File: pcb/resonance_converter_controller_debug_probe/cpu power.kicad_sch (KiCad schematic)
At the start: 9 parts, among them U30 OSD32MP157C-512M-BAA

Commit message: Add schematic for debug probe
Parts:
- TP1, TP2, TP3, TP4, TP5, TP6, TP7, TP8: footprint (none) -> TestPoint:TestPoint_Pad_D1.0mm
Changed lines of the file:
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@@
 			)
 		)
-		(property "Footprint" ""
+		(property "Footprint" "TestPoint:TestPoint_Pad_D1.0mm"
 			(at 106.68 123.19 0)
 			(effects
@@
 			)
 		)
-		(property "Footprint" ""
+		(property "Footprint" "TestPoint:TestPoint_Pad_D1.0mm"
 			(at 106.68 85.09 0)
 			(effects
@@
 			)
 		)
-		(property "Footprint" ""
+		(property "Footprint" "TestPoint:TestPoint_Pad_D1.0mm"
 			(at 118.11 26.67 0)
 			(effects
@@
 			)
 		)
-		(property "Footprint" ""
+		(property "Footprint" "TestPoint:TestPoint_Pad_D1.0mm"
 			(at 118.11 57.15 0)
 			(effects
@@
 			)
 		)
-		(property "Footprint" ""
+		(property "Footprint" "TestPoint:TestPoint_Pad_D1.0mm"
 			(at 106.68 110.49 0)
 			(effects
@@
 			)
 		)
-		(property "Footprint" ""
+		(property "Footprint" "TestPoint:TestPoint_Pad_D1.0mm"
 			(at 118.11 41.91 0)
 			(effects
@@
 			)
 		)
-		(property "Footprint" ""
+		(property "Footprint" "TestPoint:TestPoint_Pad_D1.0mm"
 			(at 106.68 97.79 0)
 			(effects
@@
 			)
 		)
-		(property "Footprint" ""
+		(property "Footprint" "TestPoint:TestPoint_Pad_D1.0mm"
 			(at 106.68 72.39 0)
 			(effects

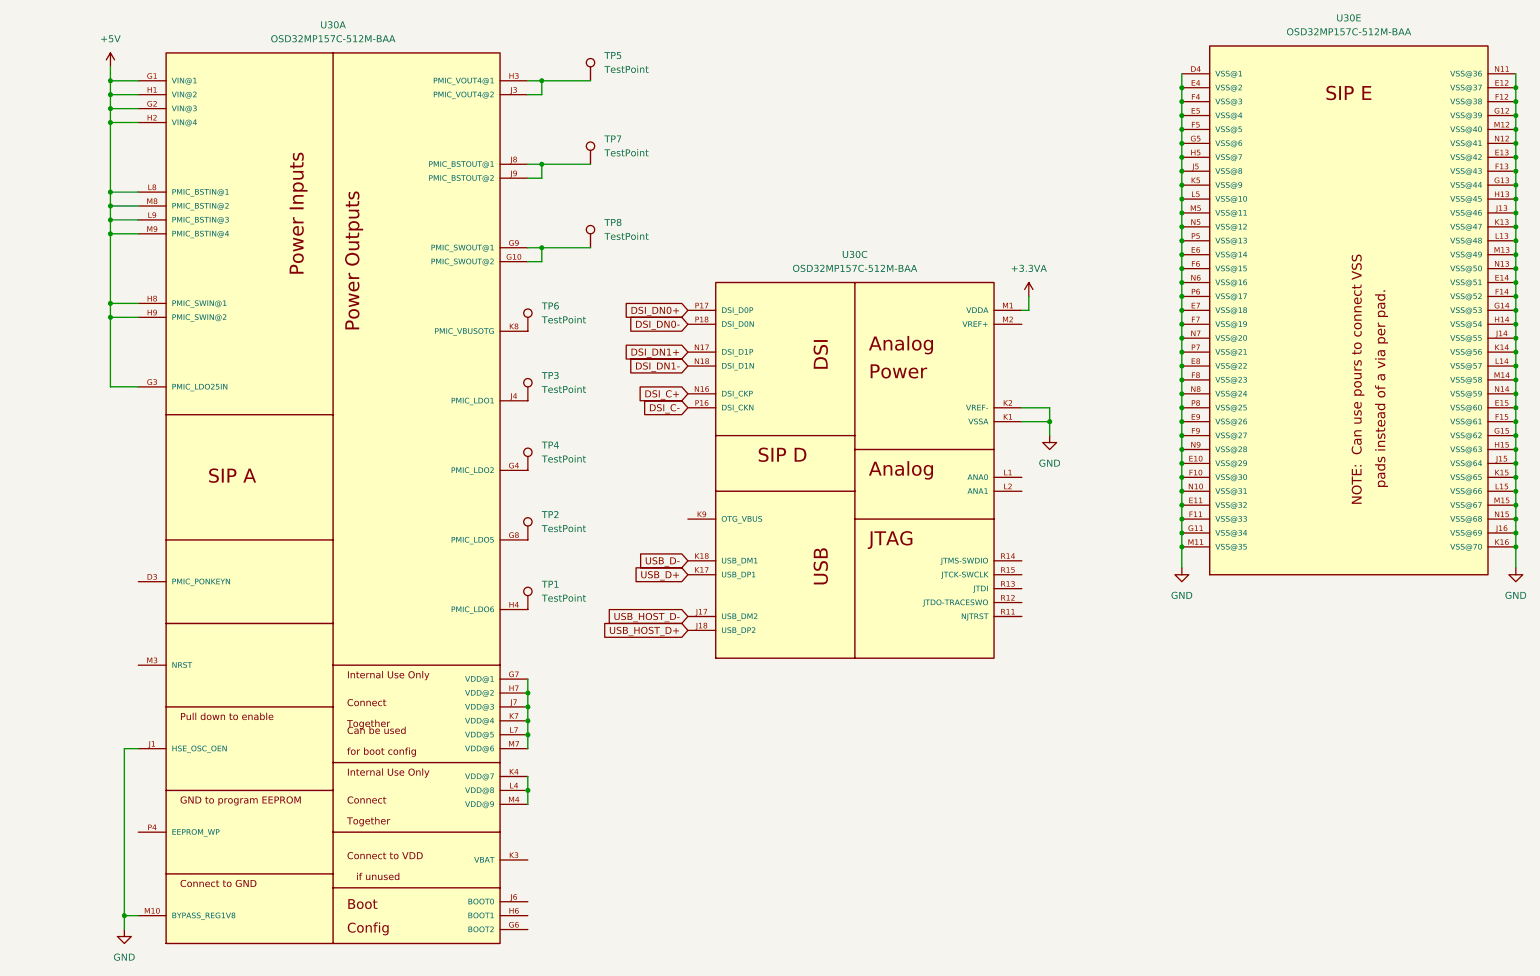
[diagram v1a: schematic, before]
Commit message: Fix schematic and initial component layout
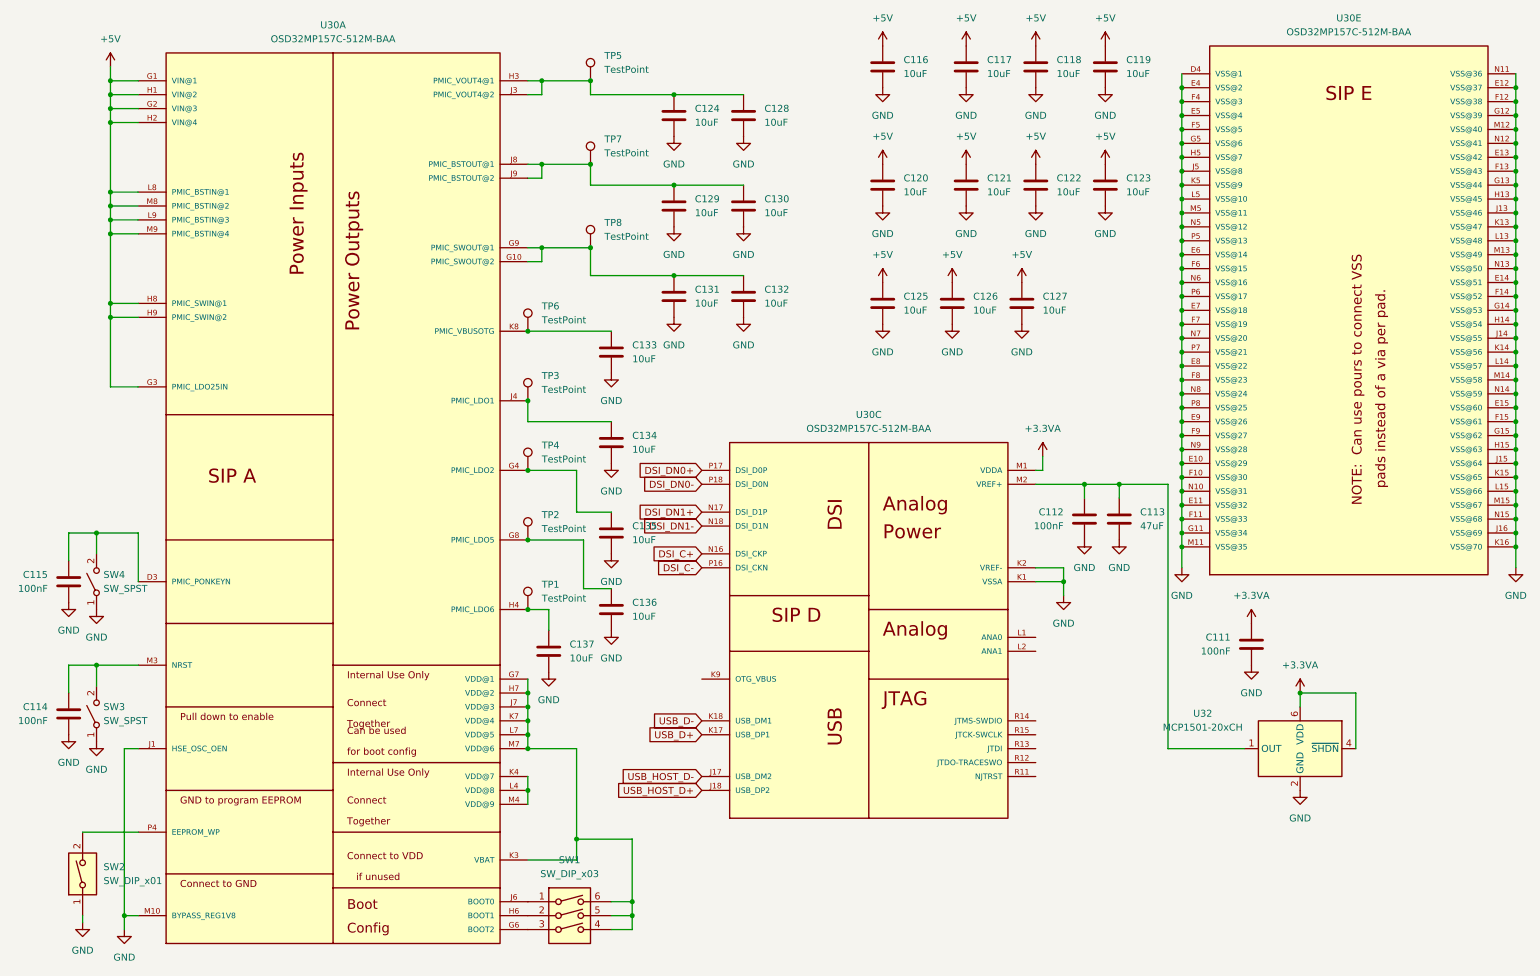
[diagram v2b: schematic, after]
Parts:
- added C111, C112, C114, C115: 100nF, Capacitor_SMD:C_0402_1005Metric, symbol Device:C
- added C113: 47uF, Capacitor_SMD:C_1206_3216Metric, symbol Device:C
- added C116, C117, C118, C119, C120, C121, C122, C123, C124, C125, C126, C127, C128, C129, C130, C131, C132, C133, C134, C135, C136, C137: 10uF, Capacitor_SMD:C_0402_1005Metric, symbol Device:C
- added SW1: SW_DIP_x03, Button_Switch_SMD:SW_DIP_SPSTx03_Slide_Omron_A6S-310x_W8.9mm_P2.54mm, symbol Switch:SW_DIP_x03
- added SW2: SW_DIP_x01, Button_Switch_SMD:SW_DIP_SPSTx01_Slide_Omron_A6S-110x_W8.9mm_P2.54mm, symbol Switch:SW_DIP_x01
- added SW3, SW4: SW_SPST, Button_Switch_SMD:SW_SPST_Omron_B3FS-100xP, symbol Switch:SW_SPST
- added U32: MCP1501-20xCH, Package_TO_SOT_SMD:SOT-23-6, symbol Reference_Voltage:MCP1501-20xCH
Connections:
- net +3.3VA: now also C111.1, U32.4 (~{SHDN}), U32.6 (VDD)
- net +5V: now also C116.1, C117.1, C118.1, C119.1, C120.1, C121.1, C122.1, C123.1, C125.1, C126.1, C127.1
- net GND: now also C111.2, C112.2, C113.2, C114.2, C115.2, C116.2, C117.2, C118.2, C119.2, C120.2, C121.2, C122.2, C123.2, C124.2, C125.2, C126.2, C127.2, C128.2, C129.2, C130.2, C131.2, C132.2, C133.2, C134.2, C135.2, C136.2, C137.2, SW2.1, SW3.1 (A), SW4.1 (A), U32.2 (GND), U32.3 (GND), U32.5 (GND)
- net at TP1.1, U30.H4 (PMIC_LDO6): now also C137.1
- net at TP3.1, U30.J4 (PMIC_LDO1): now also C134.1
- net at TP5.1, U30.H3 (PMIC_VOUT4@1), U30.J3 (PMIC_VOUT4@2): now also C124.1, C128.1
- net at TP8.1, U30.G10 (PMIC_SWOUT@2), U30.G9 (PMIC_SWOUT@1): now also C131.1, C132.1
- net at TP2.1, U30.G8 (PMIC_LDO5): now also C136.1
- net at U30.D3 (PMIC_PONKEYN): now also C115.1, SW4.2 (B)
- net at TP4.1, U30.G4 (PMIC_LDO2): now also C135.1
- net at U30.G6 (BOOT2): now also SW1.3
- net at U30.G7 (VDD@1), U30.H7 (VDD@2), U30.J7 (VDD@3)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: now also U30.K3 (VBAT), SW1.4, SW1.5, SW1.6
- net at U30.H6 (BOOT1): now also SW1.2
- net at U30.J6 (BOOT0): now also SW1.1
- net at TP7.1, U30.J8 (PMIC_BSTOUT@1), U30.J9 (PMIC_BSTOUT@2): now also C129.1, C130.1
- net at TP6.1, U30.K8 (PMIC_VBUSOTG): now also C133.1
- net at U30.M3 (NRST): now also C114.1, SW3.2 (B)
- net at U30.P4 (EEPROM_WP): now also SW2.2
- net at U30.M2 (VREF+): now also C112.1, C113.1, U32.1 (OUT)
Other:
- moved on the sheet: U30C
